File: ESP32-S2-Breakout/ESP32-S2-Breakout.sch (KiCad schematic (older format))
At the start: 36 parts, among them J1 USB_B_Micro, J3 Conn_01x23, SW1 Reset, SW2 Boot, U1 USBLC6-2SC6, U2 ESP32-S2-WROOM, U3 XC6220B331MR, Y1 32.768KHz

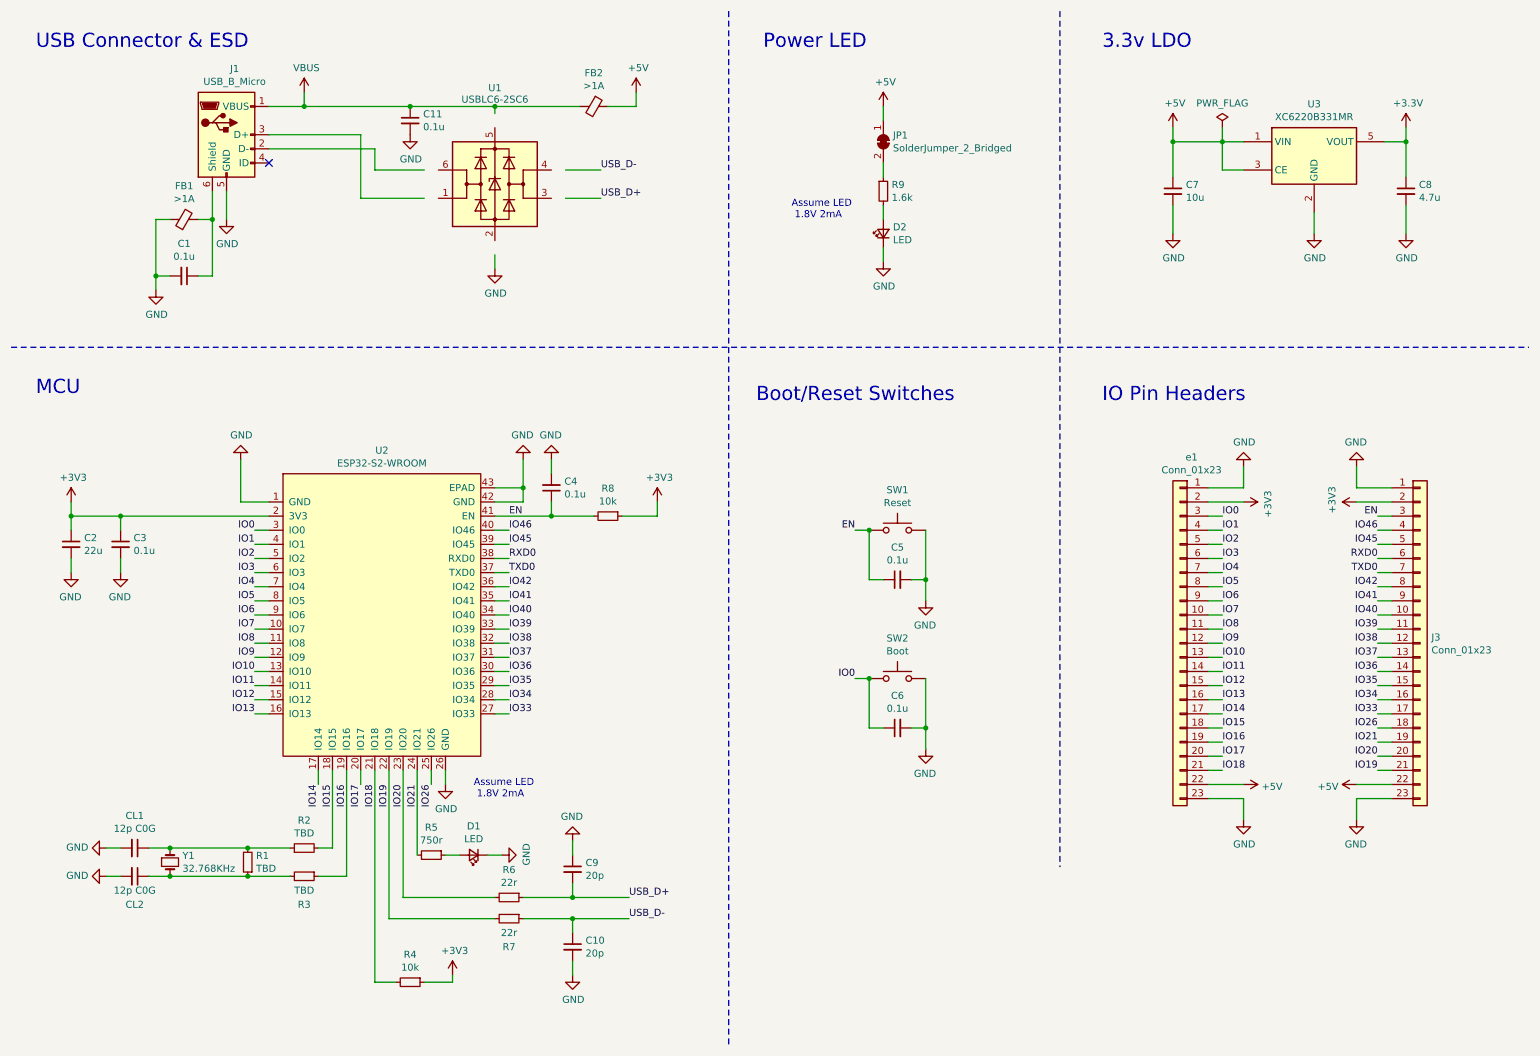
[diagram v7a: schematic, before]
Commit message: Update USB TVS
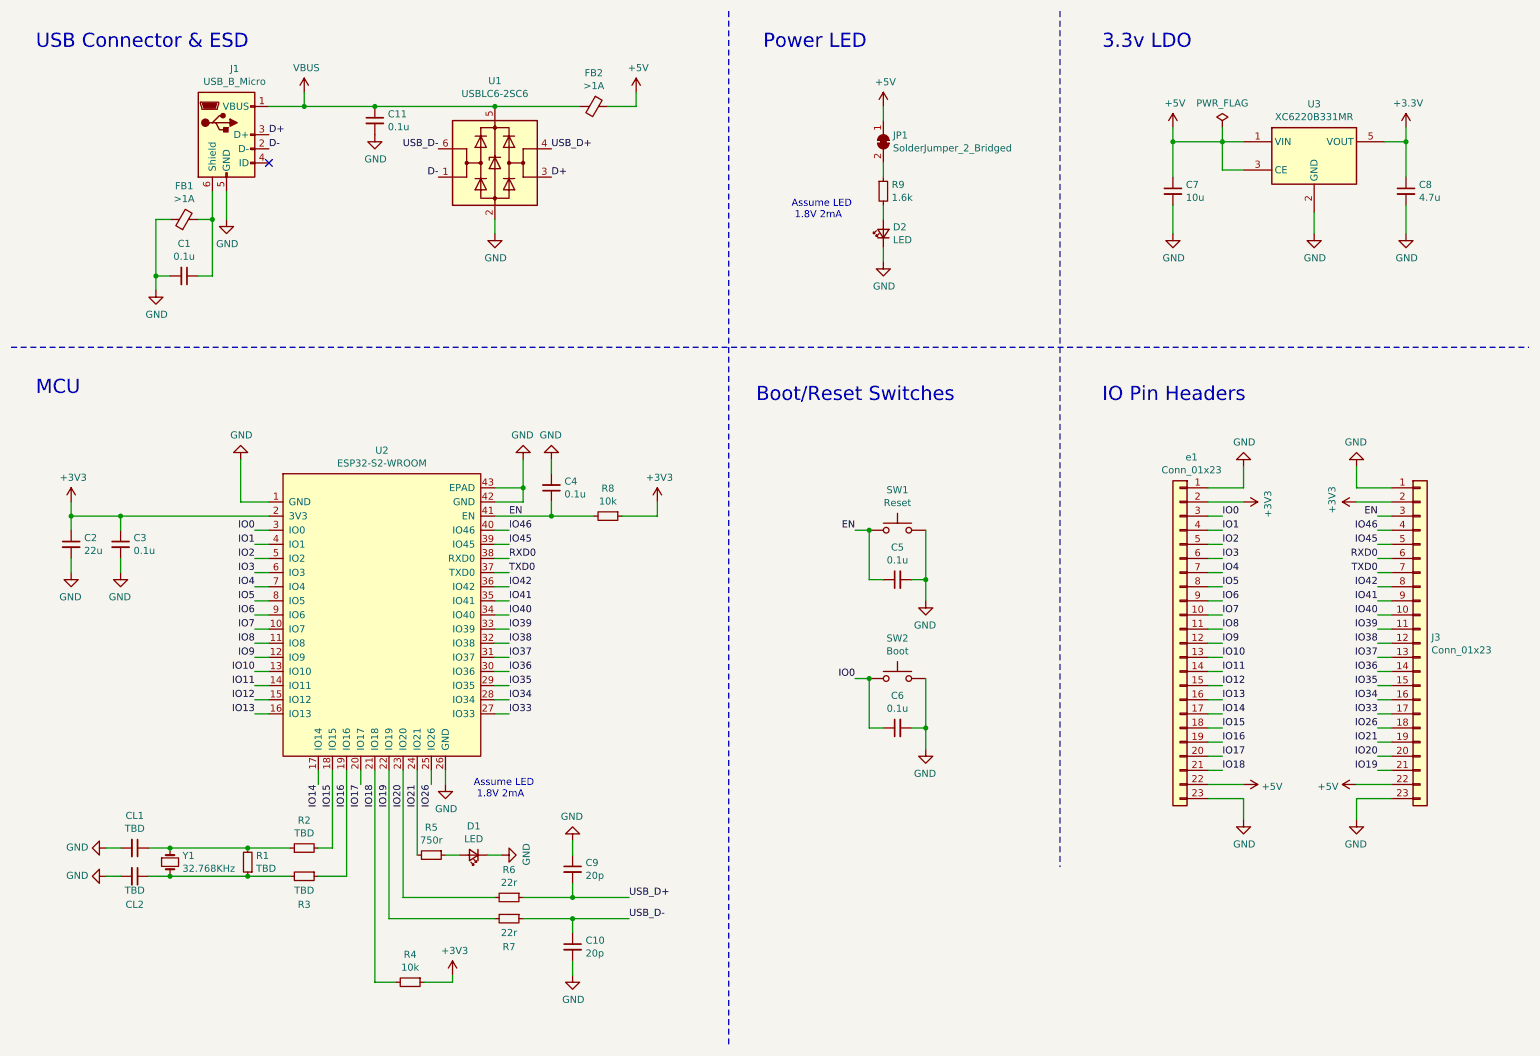
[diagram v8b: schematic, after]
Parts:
- CL1, CL2: value 12p C0G -> TBD
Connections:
- net GND: now also U1.2 (GND)
- net USB_D+: now also U1.4 (I/O2)
- net USB_D-: now also U1.6 (I/O1)
- net VBUS: now also U1.5 (VBUS)
- net D-: now reaches U1.1 (I/O1)
- net D-: now also J1.2 (D-)
- net D+: now reaches U1.3 (I/O2)
- net D+: now also J1.3 (D+)
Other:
- moved on the sheet: C11
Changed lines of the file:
@@
 AR Path="/5E6BFAB5/5E7FC96C" Ref="CL?"  Part="1"
 F 0 "CL1" V 1121 6400 50  0000 C CNN
-F 1 "12p C0G" V 1212 6400 50  0000 C CNN
+F 1 "TBD" V 1212 6400 50  0000 C CNN
 F 2 "Capacitor_SMD:C_0805_2012Metric" H 1350 6400 50  0001 C CNN
 F 3 "~" H 1350 6400 50  0001 C CNN
@@
 AR Path="/5E6BFAB5/5E7FC972" Ref="CL?"  Part="1"
 F 0 "CL2" V 1550 6600 50  0000 C CNN
-F 1 "12p C0G" V 1450 6600 50  0000 C CNN
+F 1 "TBD" V 1450 6600 50  0000 C CNN
 F 2 "Capacitor_SMD:C_0805_2012Metric" H 1350 6600 50  0001 C CNN
 F 3 "~" H 1350 6600 50  0001 C CNN
@@
 	0    1    1    0
 $EndComp
-Text Label 4650 1800 0    50   ~ 0
+Text Label 4300 1450 0    50   ~ 0
 USB_D+
-Text Label 4650 1600 0    50   ~ 0
+Text Label 3500 1450 2    50   ~ 0
 USB_D-
 $Comp
 L power:GND #PWR010
 U 1 1 5E7D59E2
-P 3900 2300
-F 0 "#PWR010" H 3900 2050 50  0001 C CNN
-F 1 "GND" H 3905 2127 50  0000 C CNN
-F 2 "" H 3900 2300 50  0001 C CNN
-F 3 "" H 3900 2300 50  0001 C CNN
-	1    3900 2300
+P 3900 2050
+F 0 "#PWR010" H 3900 1800 50  0001 C CNN
+F 1 "GND" H 3905 1877 50  0000 C CNN
+F 2 "" H 3900 2050 50  0001 C CNN
+F 3 "" H 3900 2050 50  0001 C CNN
+	1    3900 2050
 	1    0    0    -1
 $EndComp
@@
 Wire Wire Line
 	1500 2350 1500 2450
-$Comp
-L Power_Protection:USBLC6-2SC6 U1
-U 1 1 5E6F9B95
-P 3900 1700
-F 0 "U1" H 3900 2381 50  0000 C CNN
-F 1 "USBLC6-2SC6" H 3900 2300 50  0000 C CNN
-F 2 "Package_TO_SOT_SMD:SOT-23-6" H 3150 2100 50  0001 C CNN
-F 3 "http://www2.st.com/resource/en/datasheet/CD00050750.pdf" H 4100 2050 50  0001 C CNN
-	1    3900 1700
-	1    0    0    -1
-$EndComp
 Wire Wire Line
 	2300 1150 2550 1150
-Wire Wire Line
-	4400 1600 4650 1600
-Wire Wire Line
-	4650 1800 4400 1800
-Wire Wire Line
-	2300 1450 3050 1450
-Wire Wire Line
-	2300 1350 2950 1350
-Wire Wire Line
-	2950 1350 2950 1800
-Wire Wire Line
-	2950 1800 3400 1800
 Wire Wire Line
 	4700 1150 4900 1150
@@
 L Device:C_Small C11
 U 1 1 5E7A0174
-P 3300 1250
+P 3050 1250
 AR Path="/5E7A0174" Ref="C11"  Part="1"
 AR Path="/5E6BFAB5/5E7A0174" Ref="C?"  Part="1"
-F 0 "C11" H 3392 1296 50  0000 L CNN
-F 1 "0.1u" H 3392 1205 50  0000 L CNN
-F 2 "Capacitor_SMD:C_0805_2012Metric" H 3300 1250 50  0001 C CNN
-F 3 "~" H 3300 1250 50  0001 C CNN
-	1    3300 1250
-	1    0    0    -1
-$EndComp
-Wire Wire Line
-	3050 1450 3050 1600
-Wire Wire Line
-	3050 1600 3400 1600
-Connection ~ 3300 1150
+F 0 "C11" H 3142 1296 50  0000 L CNN
+F 1 "0.1u" H 3142 1205 50  0000 L CNN
+F 2 "Capacitor_SMD:C_0805_2012Metric" H 3050 1250 50  0001 C CNN
+F 3 "~" H 3050 1250 50  0001 C CNN
+	1    3050 1250
+	1    0    0    -1
+$EndComp
 $Comp
 L power:GND #PWR019
 U 1 1 5E7E803E
-P 3300 1350
-F 0 "#PWR019" H 3300 1100 50  0001 C CNN
-F 1 "GND" H 3305 1177 50  0000 C CNN
-F 2 "" H 3300 1350 50  0001 C CNN
-F 3 "" H 3300 1350 50  0001 C CNN
-	1    3300 1350
-	1    0    0    -1
-$EndComp
-Wire Wire Line
-	3900 2200 3900 2300
-Wire Wire Line
-	3300 1150 3900 1150
-Wire Wire Line
-	3900 1200 3900 1150
+P 3050 1350
+F 0 "#PWR019" H 3050 1100 50  0001 C CNN
+F 1 "GND" H 3055 1177 50  0000 C CNN
+F 2 "" H 3050 1350 50  0001 C CNN
+F 3 "" H 3050 1350 50  0001 C CNN
+	1    3050 1350
+	1    0    0    -1
+$EndComp
+Wire Wire Line
+	3900 1950 3900 2050
 Connection ~ 3900 1150
 Wire Wire Line
-	2550 1150 3300 1150
+	2550 1150 3050 1150
 Wire Wire Line
 	3900 1150 4500 1150
@@
 	1    0    0    -1
 $EndComp
+$Comp
+L Power_Protection:USBLC6-2SC6 U1
+U 1 1 5F51305D
+P 3900 1550
+F 0 "U1" H 3900 2131 50  0000 C CNN
+F 1 "USBLC6-2SC6" H 3900 2040 50  0000 C CNN
+F 2 "Package_TO_SOT_SMD:SOT-23-6" H 3900 1050 50  0001 C CNN
+F 3 "https://www.st.com/resource/en/datasheet/usblc6-2.pdf" H 4100 1900 50  0001 C CNN
+	1    3900 1550
+	1    0    0    -1
+$EndComp
+Connection ~ 3050 1150
+Wire Wire Line
+	3050 1150 3900 1150
+Text Label 2300 1350 0    50   ~ 0
+D+
+Text Label 4300 1650 0    50   ~ 0
+D+
+Text Label 2300 1450 0    50   ~ 0
+D-
+Text Label 3500 1650 2    50   ~ 0
+D-
 $EndSCHEMATC
